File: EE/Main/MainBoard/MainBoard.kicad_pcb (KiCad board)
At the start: 2 copper layers, 135.8 x 87.5 mm, 59 parts, among them J1 Conn_01x04_Male, J2 Conn_01x04_Male, J3 Conn_01x04_Male, J4 Conn_01x04_Male, J5 Conn_01x04_Male, J6 Conn_01x04_Male, J7 TAG_CONNECT, J8 Conn_01x02_Male, P1 USB_C_Plug_USB2.0, Q1 2N7002NXAKR, Q2 2N7002NXAKR, Q3 2N7002NXAKR, Q4 2N7002NXAKR, SW1 EG1206A, U1 STM32C011F4U6TR, U2 DA04-11EWA, U3 DA04-11GWA, U4 MCP73832-2-OT, U5 TPS62172DSG

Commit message: Routine Update
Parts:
- added ?: , , F.Cu at (159.6, 133.3)
- added ?: , , F.Cu at (186.3, 67.2)
- added ?: , , F.Cu at (77.0, 89.9)
- added ?: , , F.Cu at (76.4, 98.4)
- added ?: , , F.Cu at (100.4, 122.5)
- added ?: , , F.Cu at (210.3, 91.2)
- added ?: , , F.Cu at (127.1, 56.3)
- added ?: , , F.Cu at (185.5, 123.7)
- added ?: , , F.Cu at (161.1, 56.3)
- added ?: , , F.Cu at (125.6, 133.3)
- added ?: , , F.Cu at (209.6, 99.7)
- added ?: , , F.Cu at (101.1, 65.8)
- H1, H10, H11, H12, H2, H3, H4, H5, H6, H7, H8, H9: footprint MountingHole:MountingHole_2.5mm -> MountingHole:MountingHole_2.7mm
- moved H6 93.5 mm to (127.1, 56.3), turned to -90 degrees
- moved H11 90.6 mm to (159.6, 133.3), turned to 90 degrees
- moved H9 90.0 mm to (209.6, 99.7), turned to 135 degrees
- moved H3 87.6 mm to (101.1, 65.8), turned to -45 degrees
- moved H10 75.1 mm to (185.5, 123.7), turned to -45 degrees
- moved J2 72.2 mm to (92.4, 77.0), turned to -45 degrees
- moved J6 72.1 mm to (139.6, 131.6), turned to 90 degrees
- moved J3 72.1 mm to (147.1, 58.0), turned to -90 degrees
- moved J5 72.1 mm to (194.2, 112.6), turned to 135 degrees
- moved H5 71.0 mm to (161.1, 56.3), turned to -90 degrees
- moved H4 70.3 mm to (77.0, 89.9), turned to -45 degrees
- moved H12 66.5 mm to (125.6, 133.3), turned to 90 degrees
- moved H7 29.5 mm to (210.3, 91.2), turned to 45 degrees
- moved H8 28.5 mm to (186.3, 67.2)
- moved H1 5.64 mm to (76.4, 98.4), turned to -135 degrees
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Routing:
- net /SDA: track 293.3 -> 256.6 mm, vias 3 -> 5
- net /SCL: track 277.4 -> 262.6 mm
- net VCC: track 20.8 -> 10.4 mm
- net VBUS: track 22.2 -> 24.2 mm
- net /Power/V_PRE_REG: track 11.9 -> 10.7 mm
- net /Power/VBAT: track 87.1 -> 85.9 mm
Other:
- board size 135.8 x 87.5 mm -> 140.8 x 87.5 mm

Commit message: Random Check in
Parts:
- removed the ? at (159.6, 133.3)
- removed the ? at (186.3, 67.2)
- removed the ? at (77.0, 89.9)
- removed the ? at (76.4, 98.4)
- removed Q1, Q2, Q3, Q4: 2N7002NXAKR, Package_TO_SOT_SMD:SC-59
- removed R10, R11, R12, R13, R7, R8, R9: 560, Resistor_SMD:R_0402_1005Metric
- removed R16: 100k, Resistor_SMD:R_0402_1005Metric
- removed R17, R20: 0, Resistor_SMD:R_0402_1005Metric
- removed R4, R5, R6: 10k, Resistor_SMD:R_0402_1005Metric
- removed U3: DA04-11GWA, Display_7Segment:DA04-11CGKWA
- removed U5: TPS62172DSG, Package_SON:WSON-8-1EP_2x2mm_P0.5mm_EP0.9x1.6mm_ThermalVias
- added C7: 0.1u, Capacitor_SMD:C_0402_1005Metric, F.Cu at (98.7, 86.3)
- L1: value 2.2u -> 10u
- R14: value 20k -> 10k
- U1: value STM32C011F4U6TR -> STM32F030F4Px; footprint Package_DFN_QFN:UQFN-20_3x3mm_P0.4mm -> Package_SO:TSSOP-20_4.4x6.5mm_P0.65mm
- U2: value DA04-11EWA -> LM3670MF-3.3; footprint Display_7Segment:DA04-11SURKWA -> Package_TO_SOT_SMD:TSOT-23-5
- moved R3 77.2 mm to (98.5, 84.8), turned to 0 degrees
- moved U2 20.3 mm to (173.5, 117.8), turned to 0 degrees
- moved C4 13.9 mm to (172.5, 113.8), turned to 90 degrees
- moved C1 12.2 mm to (108.5, 86.0), turned to -90 degrees
- moved U1 12.1 mm to (103.7, 85.8), turned to 0 degrees
- moved J7 11.8 mm to (111.2, 75.8), turned to 90 degrees
- moved R2 11.7 mm to (110.5, 84.8), turned to 90 degrees
- moved L1 10.9 mm to (178.0, 116.8), turned to 0 degrees
- moved C5 10.4 mm to (175.0, 121.1)
- moved R1 10.2 mm to (110.5, 82.8), turned to -90 degrees
- moved C6 9.62 mm to (177.0, 121.3)
- moved R18 1.25 mm to (142.0, 112.2)
- moved R15 0.39 mm to (111.0, 121.5)
- moved R19 0.26 mm to (144.5, 112.8)
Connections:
- C4 pad 1: /Power/V_PRE_REG -> /Power/V_DISPLAY
- R3 pad 1: /Display/D1_R_EN -> VCC
- R3 pad 2: GND -> Net-(R3-Pad2)
- SW1 pad 2: /Power/V_PRE_REG -> /Power/V_DISPLAY
- U1 pad 10: /Display/G_EN -> unconnected-(U1-Pad10)
- U1 pad 11: /Display/A_EN -> /MCU/DNC_SPI_CLK
- U1 pad 12: /Display/F_EN -> unconnected-(U1-Pad12)
- U1 pad 13: /Display/B_EN -> /Display/DISPLAY_DIN
- U1 pad 14: /Display/D2_R_EN -> unconnected-(U1-Pad14)
- U1 pad 15: /Display/D1_R_EN -> GND
- U1 pad 16: /MCU/SWDIO -> VCC
- U1 pad 17: /MCU/SWDCLK -> /SCL
- U1 pad 18: /SCL -> /SDA
- U1 pad 19: /SDA -> /MCU/SWDIO
- U1 pad 2: VCC -> unconnected-(U1-Pad2)
- U1 pad 20: unconnected-(U1-Pad20) -> /MCU/SWDCLK
- U1 pad 3: GND -> unconnected-(U1-Pad3)
- U1 pad 4: unconnected-(U1-Pad4) -> Net-(R3-Pad2)
- U1 pad 5: /Display/D2_G_EN -> VCC
- U1 pad 6: /Display/D1_G_EN -> unconnected-(U1-Pad6)
- U1 pad 7: /Display/D_EN -> unconnected-(U1-Pad7)
- U1 pad 8: /Display/E_EN -> unconnected-(U1-Pad8)
- U1 pad 9: /Display/C_EN -> unconnected-(U1-Pad9)
- U2 pad 1: /Display/C -> /Power/V_DISPLAY
- U2 pad 2: /Display/E -> GND
- U2 pad 3: /Display/D -> /Power/V_DISPLAY
- U2 pad 4: /Display/D1_R -> VCC
- U2 pad 5: /Display/D2_R -> Net-(L1-Pad1)
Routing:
- net /SCL: track 262.6 -> 0.00 mm, vias 8 -> 0
- net /SDA: track 256.6 -> 0.00 mm, vias 5 -> 0
- net /Display/D1_R_EN: track 118.9 -> 0.00 mm
- net /Display/D2_R_EN: track 105.3 -> 0.00 mm
- net /Power/VBAT: track 85.9 -> 0.00 mm
- net /Display/C: track 83.9 -> 0.00 mm
- net /Display/G: track 83.1 -> 0.00 mm
- net /Display/E: track 80.3 -> 0.00 mm
- net /Display/A: track 78.3 -> 0.00 mm
- net /Display/D: track 77.5 -> 0.00 mm
- net /Display/F: track 72.7 -> 0.00 mm
- net /Display/B: track 65.9 -> 0.00 mm
- net /Display/D2_G_EN: track 62.2 -> 0.00 mm
- net /Display/D1_G_EN: track 51.9 -> 0.00 mm
- net /Display/D_EN: track 39.3 -> 0.00 mm
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- added copper zone on F.Cu, net GND
- removed copper zone on F.Cu, net VCC

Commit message: First pass layout
Assumes using Cut-through RGB 7 Segment
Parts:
- added C10: 0.1u, Capacitor_SMD:C_0402_1005Metric, F.Cu at (136.0, 96.2)
- added C11: 4.7u, Capacitor_SMD:C_0603_1608Metric, F.Cu at (141.6, 107.7)
- added C12: 4.7u, Capacitor_SMD:C_0603_1608Metric, F.Cu at (141.6, 106.3)
- added C8: 4.7u, Capacitor_SMD:C_0603_1608Metric, F.Cu at (134.6, 107.1)
- added C9: 0.1u, Capacitor_SMD:C_0402_1005Metric, F.Cu at (136.2, 91.2)
- added End1: Peg, Library:TestPattern0, F.Cu at (97.6, 94.9)
- added J9: Conn_01x04_Male, Library:RGB_7Segment, F.Cu at (132.7, 95.2)
- added L2: 4.7u, Inductor_SMD:L_0805_2012Metric, F.Cu at (137.4, 103.7)
- added R4: 250m, Resistor_SMD:R_0805_2012Metric, F.Cu at (177.0, 131.8)
- added R5: 0, Resistor_SMD:R_0402_1005Metric_Pad0.72x0.64mm_HandSolder, F.Cu at (173.0, 131.7)
- added R8: 100k, Resistor_SMD:R_0402_1005Metric, F.Cu at (128.6, 75.9)
- added R9: 100k, Resistor_SMD:R_0402_1005Metric, F.Cu at (127.7, 75.1)
- added S0: Peg, Library:TestPattern0, F.Cu at (104.0, 91.3)
- added S1: Peg, Library:TestPattern0, F.Cu at (111.0, 91.1)
- added S10: Peg, Library:TestPattern0, F.Cu at (111.2, 98.1)
- added S11: Peg, Library:TestPattern0, F.Cu at (104.0, 98.3)
- added TP+1: TestPoint, TestPoint:TestPoint_Pad_1.5x1.5mm, F.Cu at (180.0, 131.3)
- added TP-1: TestPoint, TestPoint:TestPoint_Pad_1.5x1.5mm, F.Cu at (176.5, 128.8)
- added TPDIN1: TestPoint, TestPoint:TestPoint_Pad_1.5x1.5mm, F.Cu at (132.9, 90.0)
- added TPVBAT1: TestPoint, TestPoint:TestPoint_Pad_1.5x1.5mm, F.Cu at (170.0, 131.8)
- added TPVBUS1: TestPoint, TestPoint:TestPoint_Pad_1.5x1.5mm, F.Cu at (112.5, 129.8)
- added TPVCC1: TestPoint, TestPoint:TestPoint_Pad_1.5x1.5mm, F.Cu at (153.8, 126.3)
- added TPVd1: TestPoint, TestPoint:TestPoint_Pad_1.5x1.5mm, F.Cu at (140.6, 109.7)
- added TP_DIN_UP1: TestPoint, TestPoint:TestPoint_Pad_1.5x1.5mm, F.Cu at (132.9, 97.2)
- added TP_SCL1: TestPoint, TestPoint:TestPoint_Pad_1.5x1.5mm, F.Cu at (112.2, 67.7)
- added TP_SCL2: TestPoint, TestPoint:TestPoint_Pad_1.5x1.5mm, F.Cu at (114.4, 65.1)
- added U10: DRV5032AJDBZR, Package_TO_SOT_SMD:SOT-23, F.Cu at (94.0, 94.9)
- added U3: SN74LVC1T45DBV, Package_TO_SOT_SMD:SOT-23-6, F.Cu at (134.5, 93.7)
- added U5: MCP1640Cx-xCHY, Package_TO_SOT_SMD:SOT-23-6, F.Cu at (137.7, 106.5)
- added U6: DRV5032AJDBZR, Package_TO_SOT_SMD:SOT-23, F.Cu at (104.0, 87.7)
- added U7: DRV5032AJDBZR, Package_TO_SOT_SMD:SOT-23, F.Cu at (111.1, 87.5)
- added U8: DRV5032AJDBZR, Package_TO_SOT_SMD:SOT-23, F.Cu at (111.2, 101.7)
- added U9: DRV5032AJDBZR, Package_TO_SOT_SMD:SOT-23, F.Cu at (104.1, 101.8)
- L1: value 10u -> 4.7u
- R3: value 10k -> 100k
- moved J8 32.1 mm to (173.8, 122.5)
- moved R18 32.1 mm to (171.3, 125.4)
- moved R19 32.1 mm to (173.8, 126.0)
- moved C7 28.7 mm to (125.7, 76.6), turned to -45 degrees
- moved R3 27.1 mm to (124.6, 77.6), turned to 135 degrees
- moved C6 24.6 mm to (152.6, 123.9), turned to 180 degrees
- moved L1 23.2 mm to (156.0, 124.1), turned to 180 degrees
- moved C5 22.5 mm to (152.6, 122.5), turned to 180 degrees
- moved U1 22.4 mm to (121.8, 72.7), turned to 135 degrees
- moved C3 19.5 mm to (117.2, 109.2), turned to 90 degrees
- moved C1 19.2 mm to (118.0, 69.3), turned to 135 degrees
- moved U2 17.8 mm to (156.0, 121.0), turned to -90 degrees
- moved R2 17.2 mm to (116.2, 68.5), turned to -135 degrees
- moved C4 14.4 mm to (159.2, 119.3), turned to 0 degrees
- moved C2 14.1 mm to (112.2, 111.7), turned to 180 degrees
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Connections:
- C4 pad 1: /Power/V_DISPLAY -> /MCU/ADC_
- SW1 pad 2: /Power/V_DISPLAY -> Net-(SW1-COM)
- SW1 pad 3: unconnected-(SW1-Pad3) -> Net-(R4-Pad1)
- U1 pad 10: unconnected-(U1-Pad10) -> /MCU/Start_00
- U1 pad 13: /Display/DISPLAY_DIN -> /MCU/DISPLAY_DIN
- U1 pad 14: unconnected-(U1-Pad14) -> /MCU/End
- U1 pad 2: unconnected-(U1-Pad2) -> /MCU/DIR
- U1 pad 3: unconnected-(U1-Pad3) -> /MCU/Start_10
- U1 pad 6: unconnected-(U1-Pad6) -> /MCU/ADC
- U1 pad 8: unconnected-(U1-Pad8) -> /MCU/Start_11
- U1 pad 9: unconnected-(U1-Pad9) -> /MCU/Start_01
- U2 pad 1: /Power/V_DISPLAY -> /MCU/ADC_
- U2 pad 3: /Power/V_DISPLAY -> /MCU/ADC_
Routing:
- net VCC: track 2.28 -> 688.5 mm, vias 0 -> 8
- net /SCL: track 0.00 -> 290.1 mm, vias 0 -> 2
- net /SDA: track 0.00 -> 261.7 mm
- net /MCU/ADC_: track 0.00 -> 88.0 mm, vias 0 -> 2
- net /Power/VBAT: track 0.00 -> 85.4 mm
- net /MCU/End: track 0.00 -> 44.9 mm
- net /MCU/Start_11: track 0.00 -> 44.6 mm
- net /MCU/Start_00: track 0.00 -> 33.4 mm
- net /MCU/Start_10: track 0.00 -> 32.9 mm
- net Vdrive: track 0.00 -> 32.7 mm, vias 0 -> 4
- net /MCU/DISPLAY_DIN: track 0.00 -> 32.6 mm, vias 0 -> 2
- net VBUS: track 2.70 -> 34.2 mm, vias 0 -> 2
- net GND: track 9.17 -> 40.5 mm, vias 2 -> 24
- net /MCU/DIR: track 0.00 -> 28.0 mm
- net /MCU/Start_01: track 0.00 -> 24.8 mm
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
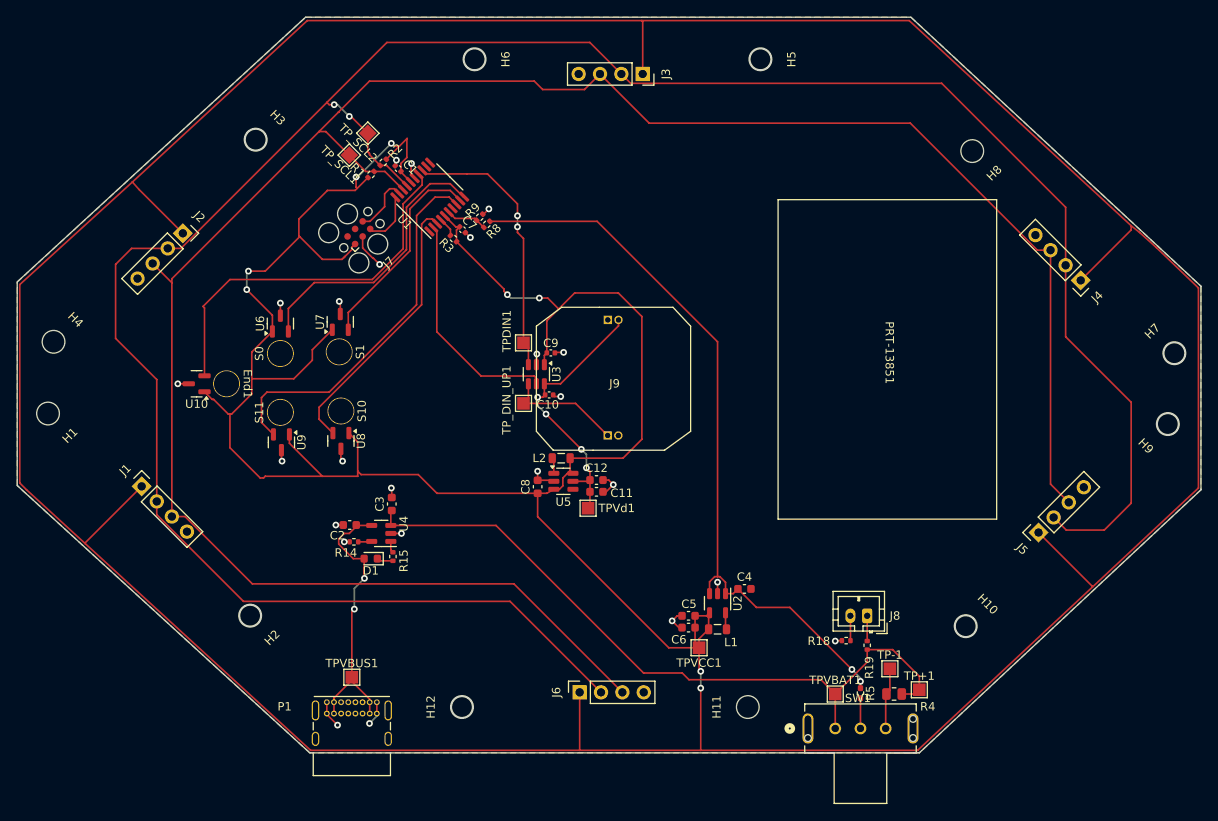
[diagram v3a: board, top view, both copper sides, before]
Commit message: Adding Ground Stitches
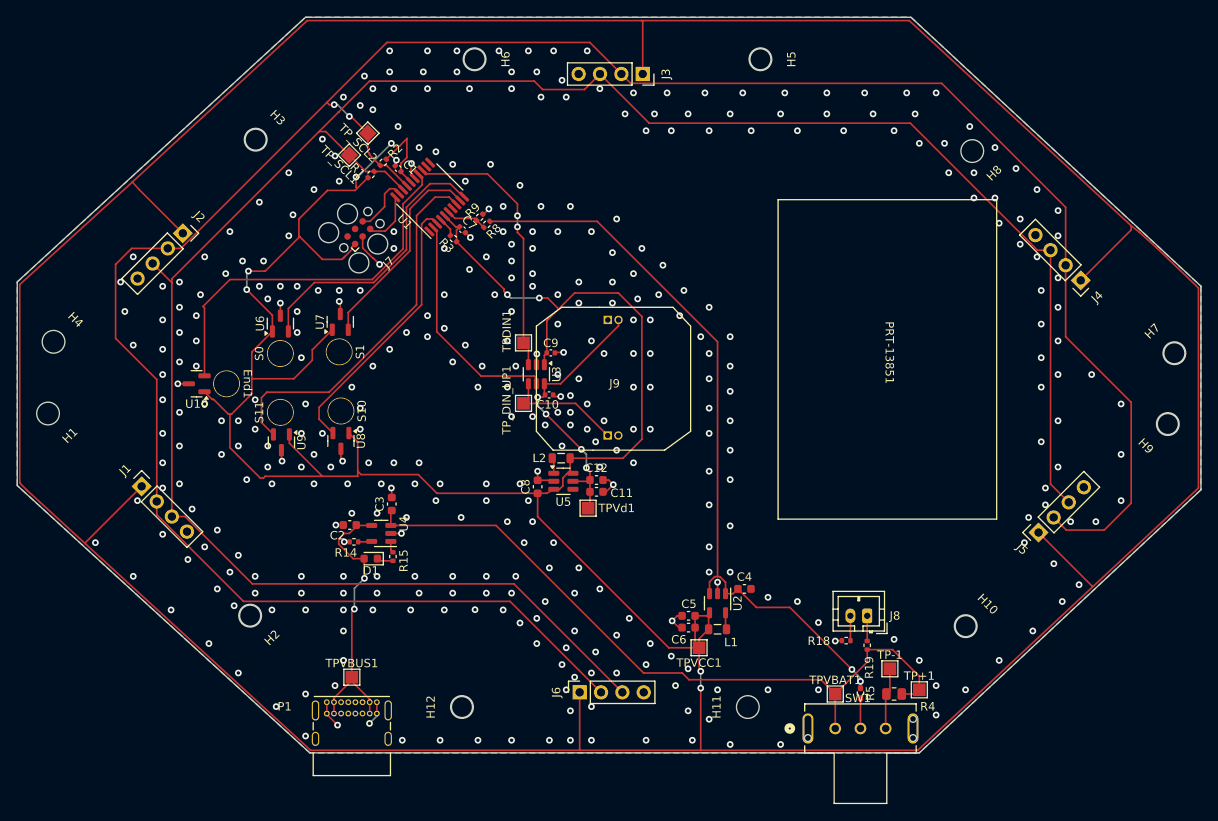
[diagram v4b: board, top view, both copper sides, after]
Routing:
- net GND: vias 24 -> 397

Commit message: Potential Layout. Need to confirm button and L&F.
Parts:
- removed TPVBAT1, TPVd1: TestPoint, TestPoint:TestPoint_Pad_1.5x1.5mm
- added C13: 8p, Capacitor_SMD:C_0402_1005Metric, F.Cu at (134.9, 71.5)
- added C14: 0.1u, Capacitor_SMD:C_0402_1005Metric, F.Cu at (107.3, 101.9)
- added C15: 0.1u, Capacitor_SMD:C_0402_1005Metric, F.Cu at (100.2, 89.4)
- added C16: 0.1u, Capacitor_SMD:C_0402_1005Metric, F.Cu at (107.8, 88.4)
- added C17: 0.1u, Capacitor_SMD:C_0402_1005Metric, F.Cu at (95.8, 98.6)
- added C5: 4.7u, Capacitor_SMD:C_0603_1608Metric, F.Cu at (143.7, 105.4)
- added C6: 4.7u, Capacitor_SMD:C_0603_1608Metric, F.Cu at (122.4, 96.8)
- added Q1: Q_PMOS_GSD, Package_TO_SOT_SMD:SOT-23, F.Cu at (113.7, 113.3)
- added Q2: Q_NMOS_GSD, Package_TO_SOT_SMD:SOT-23, F.Cu at (108.4, 112.8)
- added R10: 10k, Resistor_SMD:R_0402_1005Metric, F.Cu at (158.1, 86.4)
- added R11: 0, Resistor_SMD:R_0402_1005Metric, F.Cu at (173.9, 126.0)
- added R12: 250m, Resistor_SMD:R_0805_2012Metric, F.Cu at (117.7, 113.3)
- added R13: 10k_NP, Resistor_SMD:R_0402_1005Metric, F.Cu at (105.1, 111.8)
- added R16: 10k, Resistor_SMD:R_0402_1005Metric, F.Cu at (131.3, 68.6)
- added R17: 100k, Resistor_SMD:R_0402_1005Metric, F.Cu at (127.2, 101.1)
- added R21: 10k, Resistor_SMD:R_0402_1005Metric, F.Cu at (143.7, 108.2)
- added R22: 10k, Resistor_SMD:R_0402_1005Metric, F.Cu at (145.2, 109.2)
- added R23: 550k, Resistor_SMD:R_0402_1005Metric, F.Cu at (149.8, 107.2)
- added R24: 100k, Resistor_SMD:R_0402_1005Metric, F.Cu at (151.0, 107.2)
- added R25: 1M, Resistor_SMD:R_0402_1005Metric, F.Cu at (122.4, 93.2)
- added R26: 1M, Resistor_SMD:R_0402_1005Metric, F.Cu at (149.5, 105.7)
- added R6: 1M, Resistor_SMD:R_0402_1005Metric, F.Cu at (111.1, 113.3)
- added R7: 0, Resistor_SMD:R_0402_1005Metric, F.Cu at (171.1, 125.5)
- added TP3v1: TestPoint, TestPoint:TestPoint_Pad_1.5x1.5mm, F.Cu at (150.5, 103.7)
- added TPPGate1: TestPoint, TestPoint:TestPoint_Pad_1.5x1.5mm, F.Cu at (112.3, 110.0)
- added TPVCC1: TestPoint, TestPoint:TestPoint_Pad_1.5x1.5mm, F.Cu at (119.8, 92.7)
- added Y1: Crystal, Crystal:Crystal_SMD_5032-2Pin_5.0x3.2mm_HandSoldering, F.Cu at (131.7, 74.0)
- C12: value 4.7u -> 0.1u; footprint Capacitor_SMD:C_0603_1608Metric -> Capacitor_SMD:C_0402_1005Metric
- C3: value 4.7u -> 8p; footprint Capacitor_SMD:C_0603_1608Metric -> Capacitor_SMD:C_0402_1005Metric
- L1: value 4.7u -> 0.47u
- R15: value 2k -> 10K
- R18: value 0 -> 10K
- R19: value 0 -> 100k
- R3: value 100k -> 10k
- R4: value 250m -> 10k; footprint Resistor_SMD:R_0805_2012Metric -> Resistor_SMD:R_0402_1005Metric
- R5: value 0 -> 4.7k; footprint Resistor_SMD:R_0402_1005Metric_Pad0.72x0.64mm_HandSolder -> Resistor_SMD:R_0402_1005Metric
- SW1: value EG1206A -> SW_DPST; footprint Library:EG1206A_EWI -> Library:401-1133-ND
- U1: value STM32F030F4Px -> STM32G431K6Tx; footprint Package_SO:TSSOP-20_4.4x6.5mm_P0.65mm -> Package_QFP:LQFP-32_7x7mm_P0.8mm
- U2: value LM3670MF-3.3 -> MCP73832-2-OT; footprint Package_TO_SOT_SMD:TSOT-23-5 -> Package_TO_SOT_SMD:SOT-23-5
- U4: value MCP73832-2-OT -> ~; footprint Package_TO_SOT_SMD:SOT-23-5 -> Package_TO_SOT_SMD:SOT-583-8
- U5: value MCP1640Cx-xCHY -> LM3670MF-3.3; footprint Package_TO_SOT_SMD:SOT-23-6 -> Package_TO_SOT_SMD:TSOT-23-5
- moved TP+1 66.3 mm to (116.9, 111.0)
- moved TP-1 59.5 mm to (119.7, 111.0)
- moved R19 51.8 mm to (128.4, 101.1)
- moved SW1 48.5 mm to (152.1, 90.8)
- moved D1 43.6 mm to (157.4, 125.0), turned to 90 degrees
- moved C4 43.3 mm to (119.9, 101.1), turned to 180 degrees
- moved C3 37.2 mm to (134.9, 76.5), turned to 180 degrees
- moved R18 33.2 mm to (143.7, 107.0)
- moved U4 31.5 mm to (147.0, 106.7), turned to 0 degrees
- moved C12 27.0 mm to (114.9, 101.9)
- moved R5 22.7 mm to (154.6, 118.4), turned to 90 degrees
- moved L1 21.8 mm to (147.2, 104.2), turned to 0 degrees
- moved R4 20.6 mm to (159.2, 121.4), turned to -90 degrees
- moved U5 20.3 mm to (119.1, 98.3), turned to 90 degrees
- moved L2 20.2 mm to (119.1, 95.3), turned to 0 degrees
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- renumbered TP_SCL1 to TP_SDA1
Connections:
- C1 pad 1: VCC -> +3V3
- C12 pad 1: Vdrive -> +3V3
- C3 pad 1: /Power/VBAT -> GND
- C3 pad 2: GND -> /MCU/OSC_IN
- C5 pad 1: VCC -> +3V3
- C6 pad 1: VCC -> +3V3
- C7 pad 1: VCC -> +3V3
- C8 pad 1: VCC -> +3V3
- C9 pad 1: VCC -> +3V3
- J1 pad 1: VCC -> +3V3
- J2 pad 1: VCC -> +3V3
- J3 pad 1: VCC -> +3V3
- J4 pad 1: VCC -> +3V3
- J5 pad 1: VCC -> +3V3
- J6 pad 1: VCC -> +3V3
- J7 pad 1: VCC -> +3V3
- L1 pad 1: Net-(U2-SW) -> /MCU/ADC_
- L1 pad 2: VCC -> Net-(U4-SW)
- L2 pad 1: VCC -> Net-(U5-SW)
- L2 pad 2: Net-(U5-SW) -> +3V3
- R1 pad 1: VCC -> +3V3
- R14 pad 1: Net-(U4-PROG) -> /Power/N_SOURCE
- R15 pad 1: Net-(U4-STAT) -> +3V3
- R15 pad 2: Net-(D1-K) -> /MCU/N_GATE
- R18 pad 1: GND -> +3V3
- R18 pad 2: Net-(J8-Pin_2) -> /MCU/DISP_EN
- R19 pad 1: Net-(J8-Pin_1) -> /MCU/DIR
- R19 pad 2: /Power/VBAT -> GND
- R2 pad 1: VCC -> +3V3
- R3 pad 1: VCC -> Net-(U1-PB8)
- R3 pad 2: Net-(U1-NRST) -> GND
- R4 pad 1: Net-(R4-Pad1) -> Net-(U2-PROG)
- R4 pad 2: /Power/VBAT -> GND
- R5 pad 1: /MCU/ADC_ -> Net-(U2-STAT)
- R5 pad 2: Net-(SW1-COM) -> Net-(D1-K)
- SW1 pad 1: /Power/VBAT -> +3V3
- SW1 pad 2: Net-(SW1-COM) -> /MCU/BTN_SNS
- SW1 pad 3: Net-(R4-Pad1) -> Net-(Q1-G)
- SW1 pad 4: unconnected-(SW1-CASE-Pad4) -> Net-(R10-Pad1)
- TP+1 pad 1: /Power/VBAT -> /Power/P_DRAIN
- TP-1 pad 1: Net-(R4-Pad1) -> /MCU/ADC_
- TPVCC1 pad 1: VCC -> +3V3
- U1 pad 1: unconnected-(U1-BOOT0-Pad1) -> +3V3
- U1 pad 10: /MCU/Start_00 -> unconnected-(U1-PA5-Pad10)
- U1 pad 11: /MCU/DNC_SPI_CLK -> unconnected-(U1-PA6-Pad11)
- U1 pad 12: unconnected-(U1-PA6-Pad12) -> /MCU/N_GATE
- U1 pad 13: /MCU/DISPLAY_DIN -> /MCU/BTN_SNS
- U1 pad 14: /MCU/End -> GND
- U1 pad 15: GND -> +3V3
- U1 pad 16: VCC -> GND
- U1 pad 17: /SCL -> +3V3
- U1 pad 19: /MCU/SWDIO -> /SCL
- U1 pad 2: /MCU/DIR -> /MCU/OSC_IN
- U1 pad 20: /MCU/SWDCLK -> unconnected-(U1-PA10-Pad20)
- U1 pad 3: /MCU/Start_10 -> /MCU/OSC_OUT
- U1 pad 4: Net-(U1-NRST) -> Net-(U1-PG10)
- U1 pad 5: VCC -> /MCU/ADC
- U1 pad 6: /MCU/ADC -> unconnected-(U1-PA1-Pad6)
- U1 pad 8: /MCU/Start_11 -> /MCU/DISP_EN
- U1 pad 9: /MCU/Start_01 -> unconnected-(U1-PA4-Pad9)
- U10 pad 1: VCC -> +3V3
- U2 pad 1: /MCU/ADC_ -> Net-(U2-STAT)
- U2 pad 3: /MCU/ADC_ -> /Power/VBAT
- U2 pad 4: VCC -> VBUS
- U2 pad 5: Net-(U2-SW) -> Net-(U2-PROG)
- U3 pad 1: VCC -> +3V3
- U4 pad 1: Net-(U4-STAT) -> /MCU/ADC_
- U4 pad 2: GND -> /MCU/DISP_EN
- U4 pad 3: /Power/VBAT -> /Power/MODE
- U4 pad 4: VBUS -> Net-(U4-PG)
- U4 pad 5: Net-(U4-PROG) -> Net-(U4-FB)
- U5 pad 1: Net-(U5-SW) -> /MCU/ADC_
- U5 pad 3: VCC -> /MCU/ADC_
- U5 pad 4: Net-(U5-V_{FB}) -> +3V3
- U5 pad 5: Vdrive -> Net-(U5-SW)
- U6 pad 1: VCC -> +3V3
- U7 pad 1: VCC -> +3V3
- U8 pad 1: VCC -> +3V3
- U9 pad 1: VCC -> +3V3
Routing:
- net +3V3: track 0.00 -> 748.1 mm, vias 0 -> 14
- net VCC: track 688.5 -> 0.00 mm, vias 8 -> 0
- net /MCU/N_GATE: track 0.00 -> 77.8 mm, vias 0 -> 2
- net /MCU/BTN_SNS: track 0.00 -> 71.2 mm
- net Net-(Q1-G): track 0.00 -> 70.3 mm, vias 0 -> 2
- net /MCU/DISP_EN: track 0.00 -> 57.9 mm
- net VBUS: track 34.2 -> 81.1 mm, vias 2 -> 4
- net Vdrive: track 32.7 -> 61.2 mm, vias 4 -> 3
- net GND: track 40.5 -> 62.3 mm, vias 397 -> 371
- net /MCU/ADC: track 4.93 -> 21.7 mm, vias 0 -> 2
- net /MCU/DIR: track 28.0 -> 12.2 mm
- net /MCU/DISPLAY_DIN: track 32.6 -> 17.9 mm, vias 2 -> 0
- net /MCU/Start_00: track 33.4 -> 24.1 mm
- net /MCU/Start_01: track 24.8 -> 16.6 mm
- net /MCU/OSC_IN: track 0.00 -> 7.91 mm
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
